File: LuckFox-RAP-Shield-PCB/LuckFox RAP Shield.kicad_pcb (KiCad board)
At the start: 2 copper layers, 21.3 x 26.2 mm, 4 parts, among them J1 LuckFox_Pico_Mini_Connector, J2 External_5V_Input_from_Buck_M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, U2 W5500_Ethernet_Module_DNP_on_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

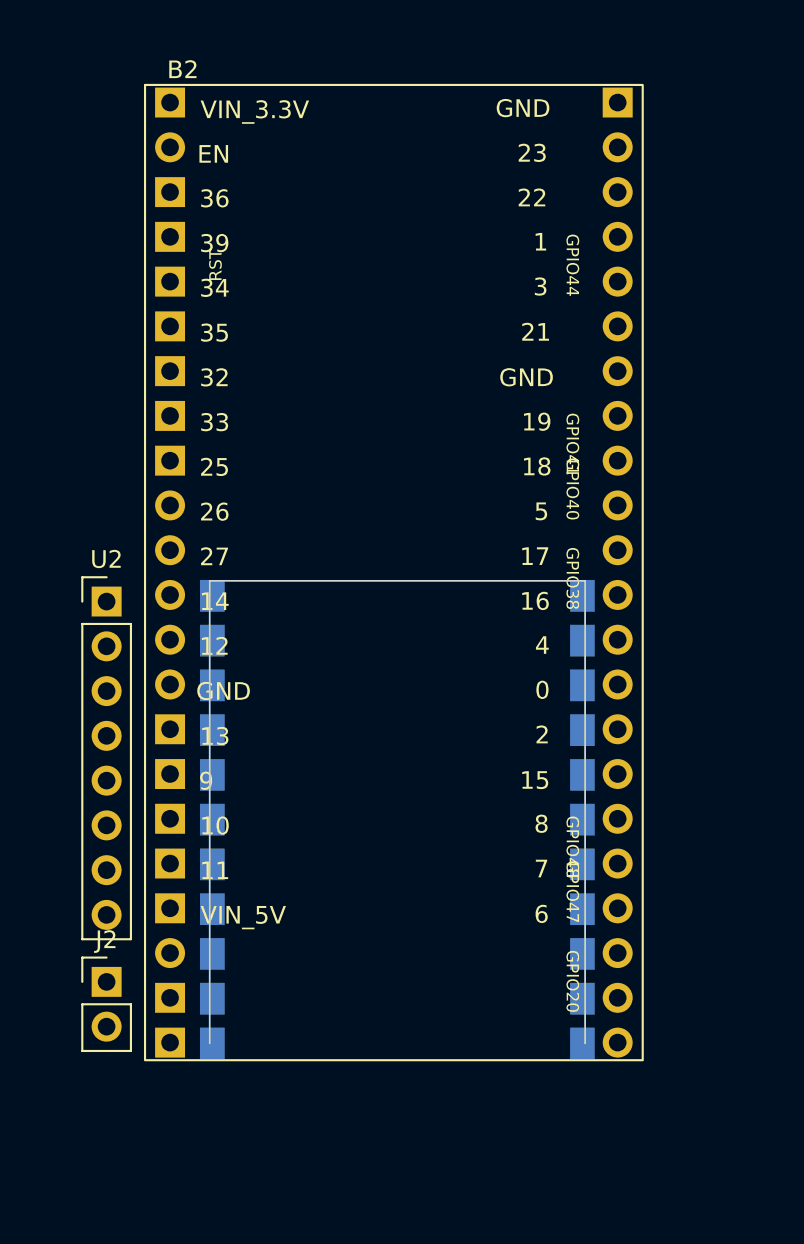
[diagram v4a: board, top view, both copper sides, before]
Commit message: Remove printed labels from PCB
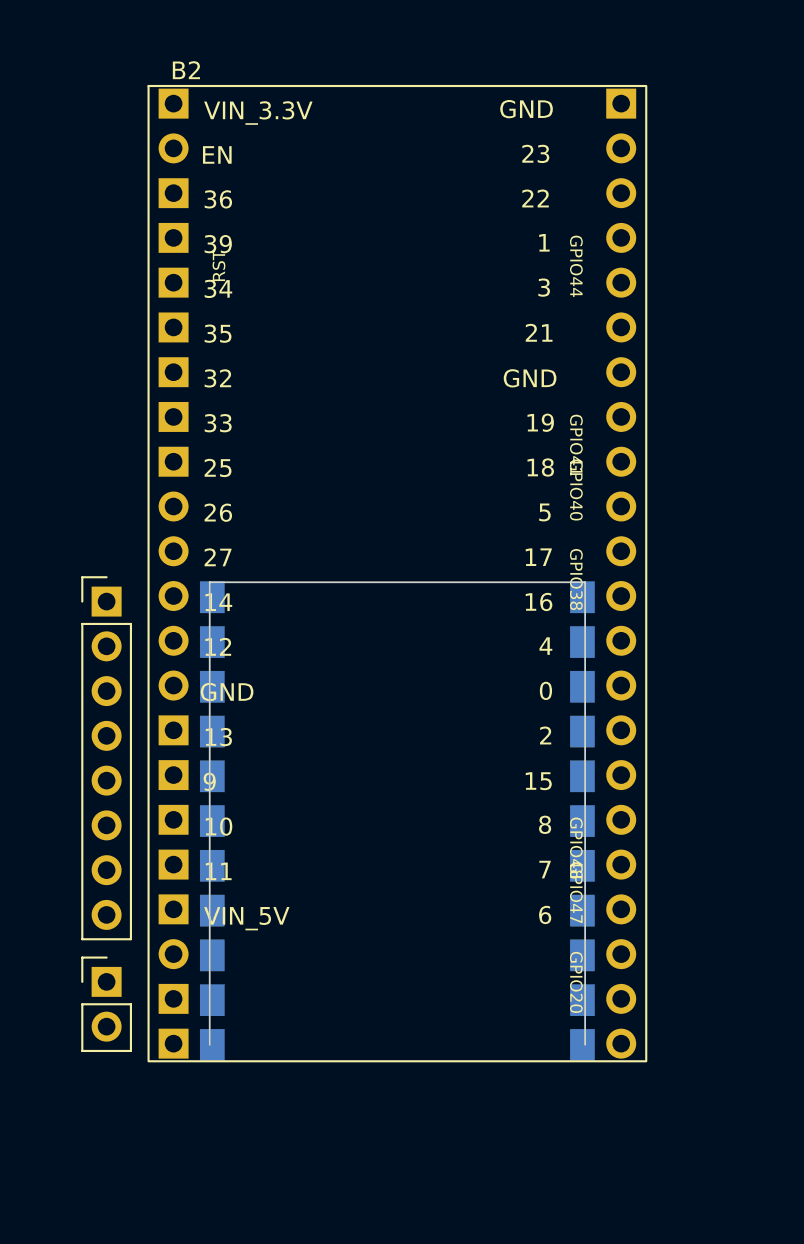
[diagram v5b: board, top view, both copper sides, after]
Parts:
- moved B2 0.21 mm to (121.5, 82.0)
- moved J1 0.08 mm to (125.0, 110.1)
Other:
- board size 21.3 x 26.2 mm -> 21.3 x 26.3 mm
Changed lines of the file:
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@@
 	(footprint "footprints:ESP32_Dev_Board_Breakout"
 		(layer "F.Cu")
-		(at 121.33 81.92)
+		(at 121.53 81.98)
 		(descr "Real ESP32-S3-WROOM-1 DevKitC-1 dual-USB-C variant, 44 pins (22/row), 2.54mm pitch, 25.40mm row spacing (1.27mm inset from each edge on a 27.94mm-wide board). Pin labels and this shield's schematic-pin-number mapping are per the board's own silkscreen GPIO numbers -- confirmed against a full pinout diagram. Board length is the pin-to-pin span (53.34mm, 21 gaps x 2.54mm, per direct user measurement) plus 0.85mm margin on each end (half the 1.7mm pad size) so the through-hole pads are physically whole rather than clipped by the board edge -- this is a normal pin-header board, not castellated.")
 		(property "Reference" "B2"
@@
 			(unlocked yes)
 			(layer "F.Fab")
+			(hide yes)
 			(effects
 				(font
@@
 		(tags "Through hole pin header THT 1x08 2.54mm single row")
 		(property "Reference" "U2"
-			(at 0 -2.38 0)
-			(layer "F.SilkS")
+			(at -7.5 3.835 0)
+			(layer "F.SilkS")
+			(hide yes)
 			(effects
 				(font
@@
 			(at 0 20.16 0)
 			(layer "F.Fab")
+			(hide yes)
 			(effects
 				(font
@@
 			)
 			(layer "F.Fab")
-		)
-		(fp_text user "${REFERENCE}"
-			(at 0 8.89 90)
-			(layer "F.Fab")
-			(effects
-				(font
-					(size 1 1)
-					(thickness 0.15)
-				)
-			)
 		)
 		(pad "1" thru_hole rect
@@
 		(tags "Through hole pin header THT 1x02 2.54mm single row")
 		(property "Reference" "J2"
-			(at 0 -2.38 0)
-			(layer "F.SilkS")
+			(at -7.5 3.835 0)
+			(layer "F.SilkS")
+			(hide yes)
 			(effects
 				(font
@@
 			(at 0 4.92 0)
 			(layer "F.Fab")
+			(hide yes)
 			(effects
 				(font
@@
 			(layer "F.Fab")
 		)
-		(fp_text user "${REFERENCE}"
-			(at 0 1.27 90)
-			(layer "F.Fab")
-			(effects
-				(font
-					(size 1 1)
-					(thickness 0.15)
-				)
-			)
-		)
 		(pad "1" thru_hole rect
 			(at 0 0)
@@
 	(footprint "footprints:LuckFox_Pico_Mini"
 		(layer "B.Cu")
-		(at 125 110.06)
+		(at 125 110.14)
 		(descr "Cutout + edge-castellation mount for LuckFox Pico Mini, MIRRORED (component side, incl. camera FPC connector, faces AWAY from the shield -- accessible from outside once assembled) -- module nests underneath the shield through this slot. Board length = the measured pin-to-pin span (25.4mm, 10 gaps x 2.54mm) plus 0.7mm margin on each end (half the 1.4mm pad height) so the top/bottom-row pads aren't clipped by the board edge -- only the left/right edges are meant to be castellated, per the module's own design. U-shaped opening: enclosed on left/right/top, OPEN on the bottom edge (the USB-C end, post-mirror) so the module's USB-C connector can extend past the shield's own board edge. The left/right enclosing walls stop exactly at the last pin row (y=26.1, pin 1/22) rather than extending through the bottom margin zone -- that margin only exists to keep the pad copper whole, not to add extra enclosed material on the open side. The open side only works if this footprint is positioned so that opening actually reaches your board's real outer edge -- it is not automatically merged with your board outline. 22 castellated edge pads lap-solder directly to the pads here -- no header/socket. Pads centered on LuckFox's nominal edge line (2.54mm pitch, 17.78mm row spacing, per LuckFox's official mechanical drawing) so they straddle the routed slot edge on the left/right. Pin-row order is reversed vs the unmirrored version: real pin 11/12 (camera-connector end) are now at the top (y=0.7), real pin 1/22 (USB-C end) now at the bottom (y=26.1). Confirm the margin/pad size against your fab house's minimum slot/annular tolerances before ordering.")
 		(property "Reference" "J1"
@@
 			(unlocked yes)
 			(layer "B.Fab")
+			(hide yes)
 			(effects
 				(font
@@
 			(layer "B.Fab")
 		)
-		(fp_text user "12"
-			(at -6.345 13.07 0)
+		(fp_text user "11"
+			(at -3.2 26.77 0)
 			(unlocked yes)
 			(layer "B.SilkS")
@@
 			)
 		)
-		(fp_text user "11"
-			(at -3.2 26.77 0)
+		(fp_text user "1"
+			(at -2.6 1.37 0)
 			(unlocked yes)
 			(layer "B.SilkS")
@@
 			)
 		)
-		(fp_text user "1"
-			(at -2.6 1.37 0)
+		(fp_text user "22"
+			(at 23.6 1.37 0)
 			(unlocked yes)
 			(layer "B.SilkS")
@@
 				)
 				(justify mirror)
-			)
-		)
-		(fp_text user "22"
-			(at 23.6 1.37 0)
-			(unlocked yes)
-			(layer "B.SilkS")
-			(effects
-				(font
-					(size 0.8 0.8)
-					(thickness 0.12)
-				)
-				(justify mirror)
-			)
-		)
-		(fp_text user "${REFERENCE}"
-			(at 10.5 14.07 0)
-			(unlocked yes)
-			(layer "B.Fab")
-			(effects
-				(font
-					(size 1 1)
-					(thickness 0.15)
-				)
-				(justify mirror)

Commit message: Draw main board outline and bump ESP32 silkscreen text to the min height
Board outline: a rectangle with a notch cut into the bottom edge, exactly
matching J1's LuckFox cutout mouth (124.85,136.24)-(146.15,136.24), so the
cutout's 3 walls merge into one closed Edge.Cuts loop with the LuckFox
module's USB-C end poking through the notch. Everywhere else the edge
sits at Y=140, clear of B2 and J2's nearest pads by several mm -- fixes
the invalid_outline/copper_edge_clearance DRC errors.

ESP32 footprint: all 44 pin-label texts were 0.7mm tall, under the
board's 0.8mm silk text height rule; bumped to 0.8mm/0.12mm thickness.
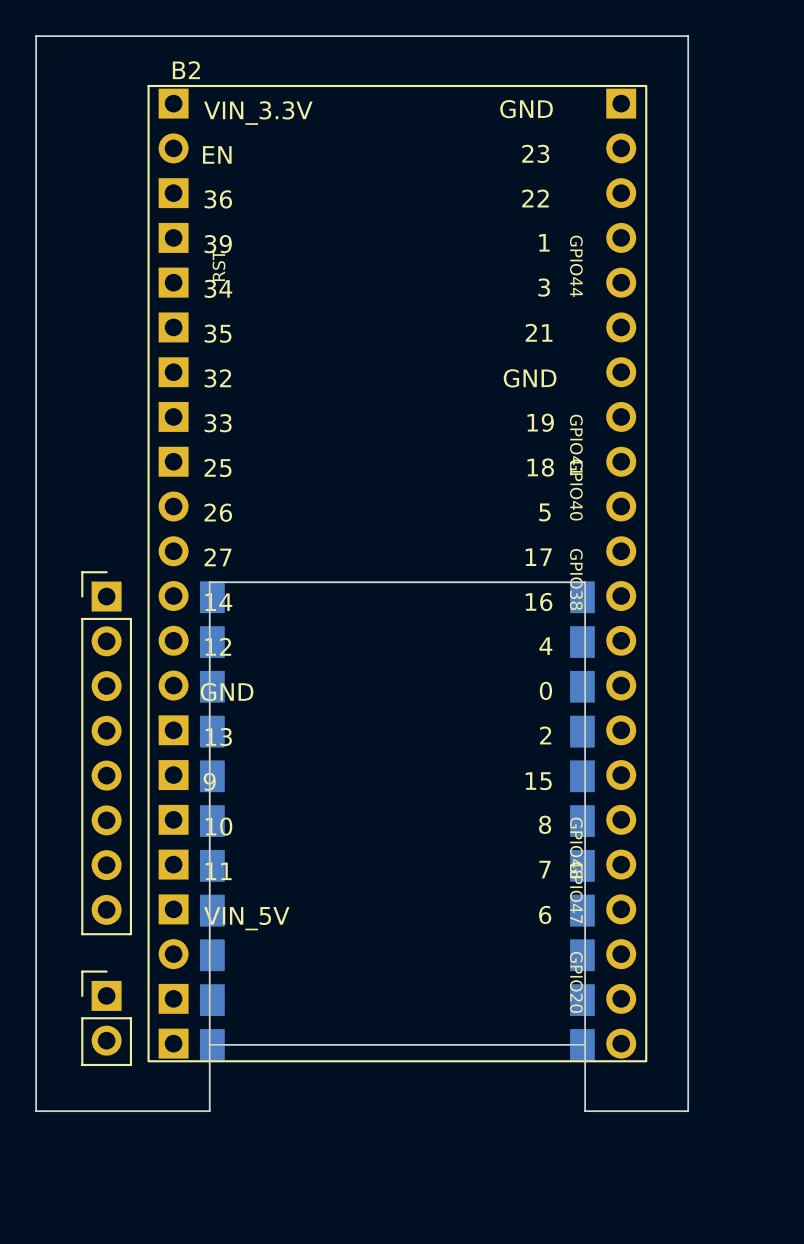
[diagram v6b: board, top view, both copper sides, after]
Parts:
- moved J2 0.80 mm to (119.0, 133.5)
- moved U2 0.28 mm to (119.0, 110.8)
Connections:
- B2 pad 10: unconnected-(B2-GPIO10_CS_ETH-Pad10) -> Net-(B2-GPIO10_CS_ETH)
- B2 pad 11: unconnected-(B2-GPIO11_MOSI_ETH-Pad11) -> Net-(B2-GPIO11_MOSI_ETH)
- B2 pad 13: unconnected-(B2-GPIO13_MISO_ETH-Pad13) -> Net-(B2-GPIO13_MISO_ETH)
- B2 pad 14: unconnected-(B2-GPIO15_DATA_RDY_IN-Pad14) -> Net-(B2-GPIO15_DATA_RDY_IN)
- B2 pad 15: unconnected-(B2-GPIO16_SLAVE_RDY_OUT-Pad15) -> Net-(B2-GPIO16_SLAVE_RDY_OUT)
- B2 pad 16: unconnected-(B2-GND-Pad16) -> GND
- B2 pad 9: unconnected-(B2-GPIO9_INT_ETH-Pad9) -> Net-(B2-GPIO9_INT_ETH)
- J1 pad 10: unconnected-(J1-GPIO1_C4_d_DATA_RDY-Pad10) -> Net-(B2-GPIO15_DATA_RDY_IN)
- J1 pad 18: unconnected-(J1-GPIO0_A4_d_SLAVE_RDY-Pad18) -> Net-(B2-GPIO16_SLAVE_RDY_OUT)
- J1 pad 21: unconnected-(J1-GND-Pad21) -> GND
- U2 pad 1: unconnected-(U2-VCC_3V3-Pad1) -> +3V3_RAIL
- U2 pad 2: unconnected-(U2-GND-Pad2) -> GND
- U2 pad 3: unconnected-(U2-RST-Pad3) -> +3V3_RAIL
- U2 pad 4: unconnected-(U2-CS-Pad4) -> Net-(B2-GPIO10_CS_ETH)
- U2 pad 6: unconnected-(U2-MOSI-Pad6) -> Net-(B2-GPIO11_MOSI_ETH)
- U2 pad 7: unconnected-(U2-MISO-Pad7) -> Net-(B2-GPIO13_MISO_ETH)
- U2 pad 8: unconnected-(U2-INT-Pad8) -> Net-(B2-GPIO9_INT_ETH)
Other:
- board size 21.3 x 26.3 mm -> 37 x 61 mm
